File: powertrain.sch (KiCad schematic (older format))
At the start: 51 parts, among them P1 TST, P10 TST, P11 TST, P12 TST, P13 TST, P14 TST, P15 TST, P16 TST, P17 TST, P2 TST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

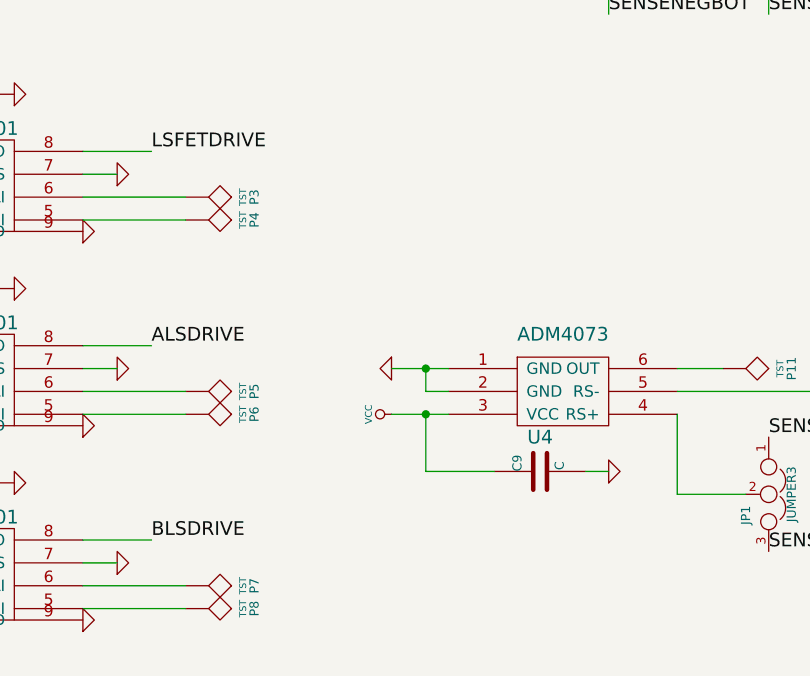
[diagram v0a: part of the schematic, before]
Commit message: changed vsense pin back to voltage divider to test webserver
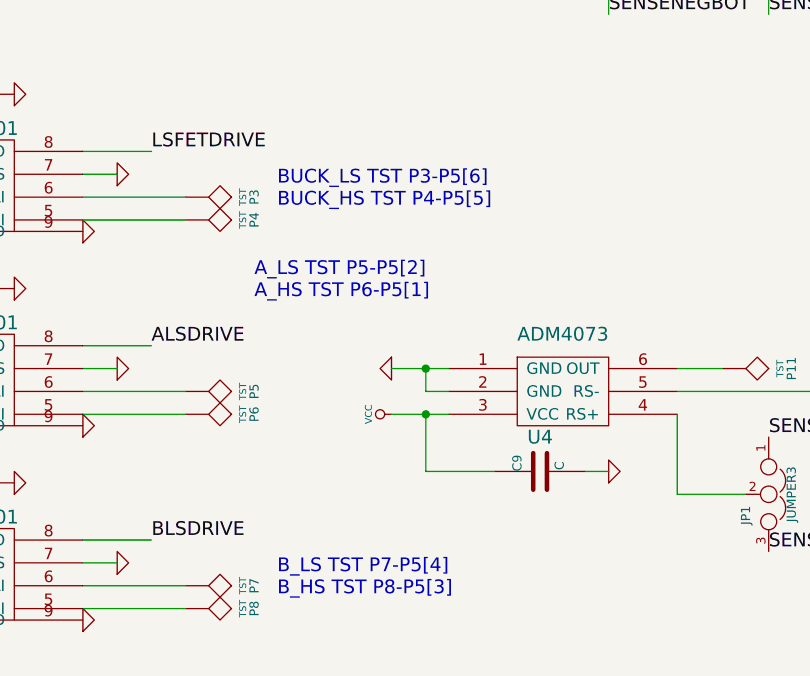
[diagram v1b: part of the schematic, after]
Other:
- note added: "A_LS TST P5-P5[2]\nA_HS TST P6-P5[1]"
- note added: "BUCK_LS TST P3-P5[6]\nBUCK_HS TST P4-P5[5]"
- note added: "B_LS TST P7-P5[4]\nB_HS TST P8-P5[3]"
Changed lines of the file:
@@
 Sheet 1 1
 Title ""
-Date "6 oct 2014"
+Date "17 nov 2014"
 Rev ""
 Comp ""
@@
 Text Label 10500 4100 0    60   ~ 0
 B
+Text Notes 3350 5300 0    60   ~ 0
+BUCK_LS TST P3-P5[6]\nBUCK_HS TST P4-P5[5]
+Text Notes 3250 5700 0    60   ~ 0
+A_LS TST P5-P5[2]\nA_HS TST P6-P5[1]
+Text Notes 3350 7000 0    60   ~ 0
+B_LS TST P7-P5[4]\nB_HS TST P8-P5[3]
 $EndSCHEMATC
